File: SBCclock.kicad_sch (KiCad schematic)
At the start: 12 parts, among them J1 Conn_01x06_Male, J2 Conn_01x06_Male, U1 74HCT04, U2 74HC163, U3 74AHC1G02, Y1 25.175MHz

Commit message: chore: tweak values
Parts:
- C2: value 18pF -> 1uF
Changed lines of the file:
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@@
       (effects (font (size 1.27 1.27)))
     )
-    (property "Value" "18pF" (at 130.1496 98.0948 90)
+    (property "Value" "1uF" (at 130.1496 98.0948 90)
       (effects (font (size 1.27 1.27)))
     )

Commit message: chore: adjust routing
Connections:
- net ~{RESET}: now reaches J2.4 (Pin_4)
- no-connect marks 8 -> 7
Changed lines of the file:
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@@
   (no_connect (at 121.2596 118.6688))
   (no_connect (at 146.6596 123.7488))
-  (no_connect (at 253.0856 41.4528))
   (wire (pts (xy 86.3092 47.498) (xy 86.3092 60.7568))
     (stroke (width 0) (type default))
@@
       (effects (font (size 1.27 1.27)) (justify left) hide)
     )
+  )
+  (global_label "~{RESET}" (shape input) (at 253.0856 41.4528 0) (fields_autoplaced)
+    (effects (font (size 1.27 1.27)) (justify left))
+    (property "Intersheetrefs" "${INTERSHEET_REFS}" (at 261.7365 41.4528 0)
+      (effects (font (size 1.27 1.27)) (justify left) hide)
+    )

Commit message: revise E generation
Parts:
- added C3: 1uF, Capacitor_SMD:C_0805_2012Metric_Pad1.18x1.45mm_HandSolder, symbol Device:C
- added D1: LED, LED_SMD:LED_0805_2012Metric_Pad1.15x1.40mm_HandSolder, symbol Device:LED_Small_Filled
- added R5: 330R, Resistor_SMD:R_0805_2012Metric_Pad1.20x1.40mm_HandSolder, symbol Device:R_Small
- added U4: 74AHC1G08, Package_TO_SOT_SMD:SOT-353_SC-70-5_Handsoldering, symbol 74xGxx:74AHC1G08
- added U5: 74AHC1G32, Package_TO_SOT_SMD:SOT-353_SC-70-5_Handsoldering, symbol 74xGxx:74AHC1G32
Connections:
- net +5V: now also C3.1, R5.2, U4.5 (VCC), U5.5 (VCC)
- net Clock3: now also U4.1
- net Clock6: now also U4.2
- net E: now also U5.4; no longer U3.4
- net GND: now also C3.2, D1.1 (K), U4.3 (GND), U5.3 (GND)
- net at C1.2, R1.1, R2.1: now also U1.3; no longer U1.1
- net at R2.2, Y1.1: now also U1.4; no longer U1.2
- net at C1.1, R3.2, U1.5: now also U1.2; no longer U1.4
- net at R3.1, Y1.2: now also U1.1; no longer U1.3
- new net: D1.2 (A), R5.1
- new net: U3.4, U5.1
- new net: U4.4, U5.2
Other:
- moved on the sheet: U3

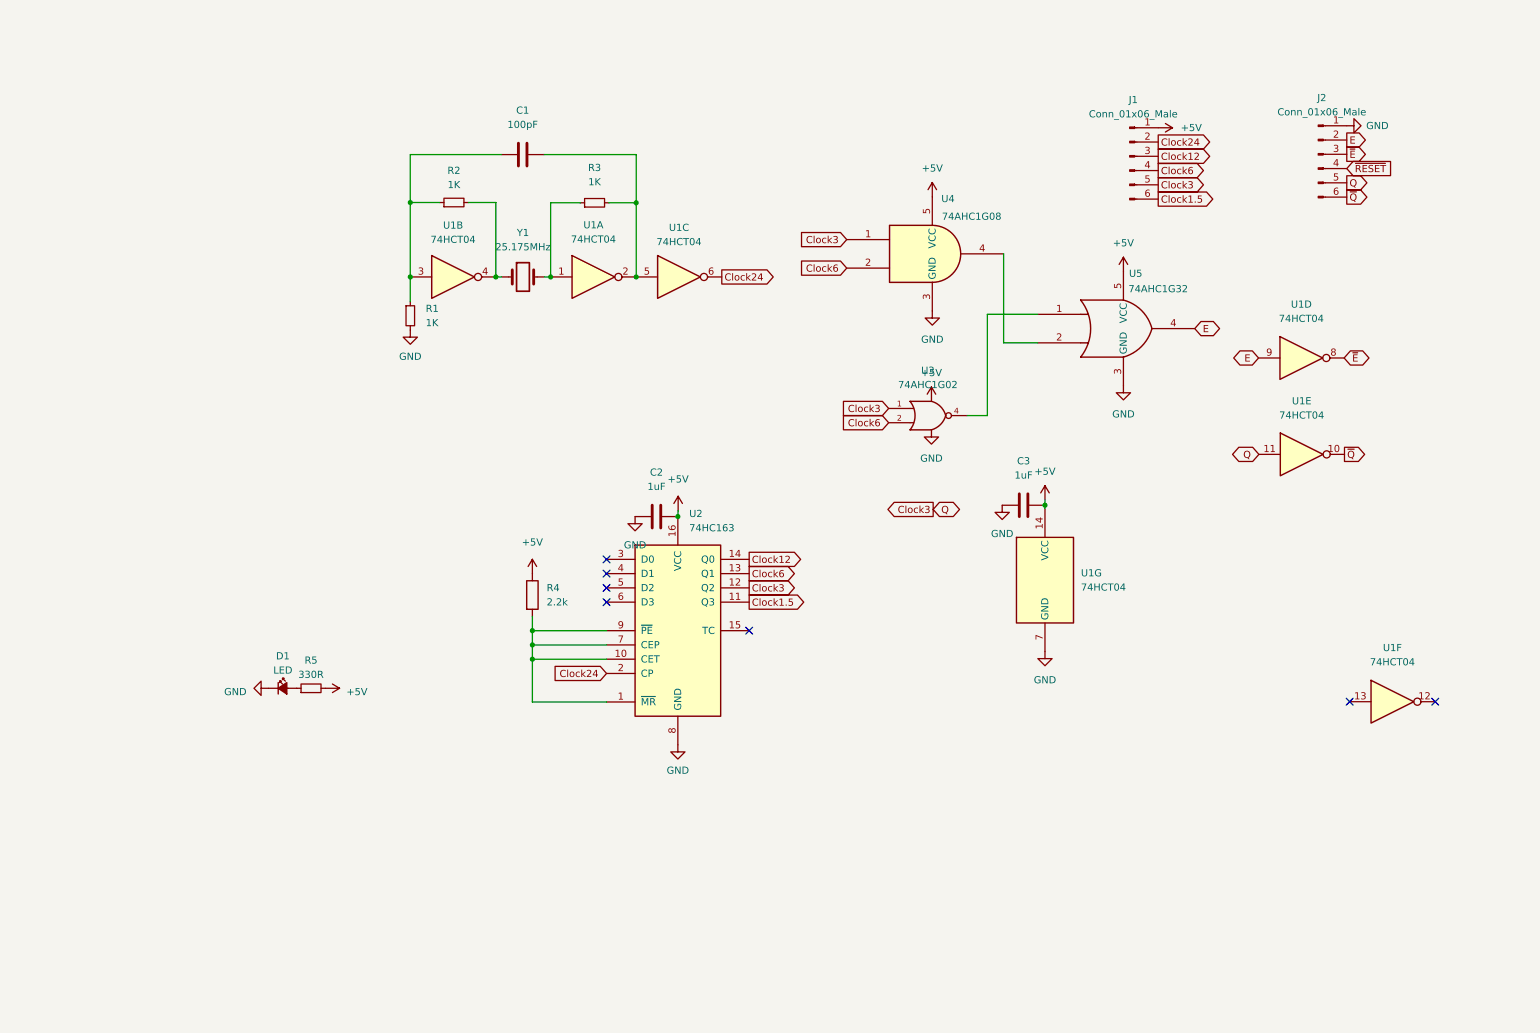
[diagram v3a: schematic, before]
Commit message: simplified board
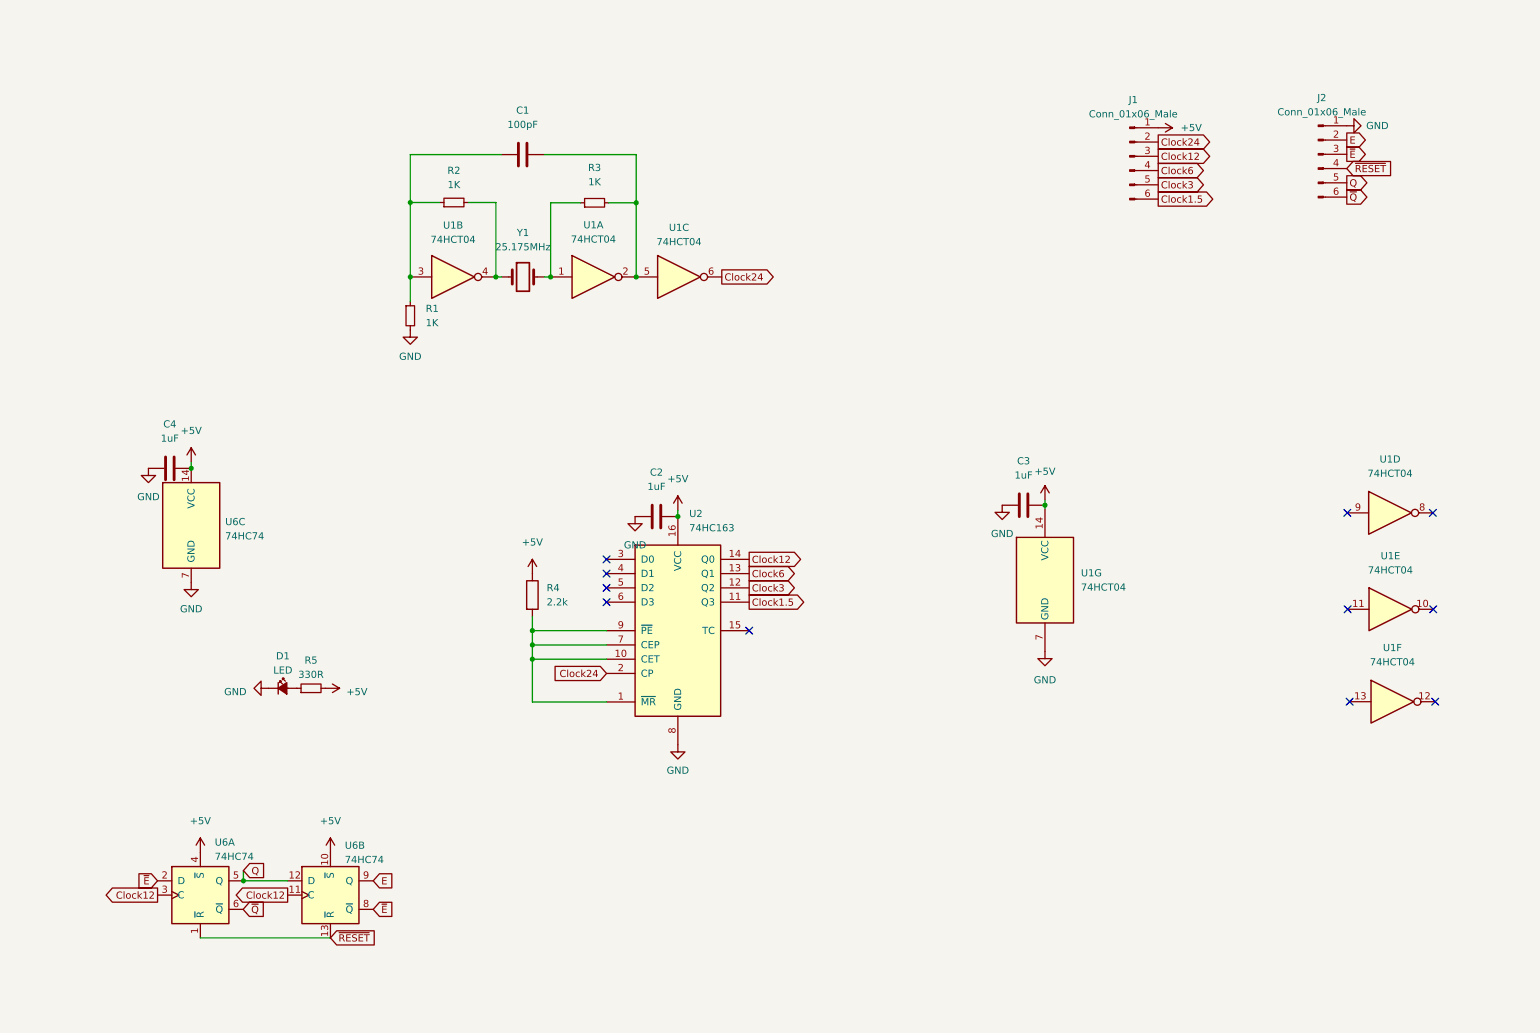
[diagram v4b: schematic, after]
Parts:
- removed U3: 74AHC1G02, Package_TO_SOT_SMD:SOT-353_SC-70-5_Handsoldering, symbol 74xGxx:74AHC1G02
- removed U4: 74AHC1G08, Package_TO_SOT_SMD:SOT-353_SC-70-5_Handsoldering, symbol 74xGxx:74AHC1G08
- removed U5: 74AHC1G32, Package_TO_SOT_SMD:SOT-353_SC-70-5_Handsoldering, symbol 74xGxx:74AHC1G32
- added C4: 1uF, Capacitor_SMD:C_0805_2012Metric_Pad1.18x1.45mm_HandSolder, symbol Device:C
- added U6: 74HC74, Package_SO:SOIC-14_3.9x8.7mm_P1.27mm, symbol 74xx:74HC74
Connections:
- net +5V: now also C4.1, U6.10 (~{S}), U6.14 (VCC), U6.4 (~{S})
- net Clock12: now also U6.11 (C), U6.3 (C)
- net Clock3: no longer J2.5 (Pin_5), U1.11
- net E: now also U6.9 (Q); no longer U1.9
- net GND: now also C4.2, U6.7 (GND)
- net ~{E}: now also U6.2 (D), U6.8 (~{Q}); no longer U1.8
- net ~{Q}: now also U6.6 (~{Q}); no longer U1.10
- net ~{RESET}: now also U6.1 (~{R}), U6.13 (~{R})
- new net Q: J2.5 (Pin_5), U6.12 (D), U6.5 (Q)
- no-connect marks 7 -> 11
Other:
- moved on the sheet: U1D, U1E

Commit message: revise clock signal
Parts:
- removed R3: 1K, Resistor_SMD:R_0805_2012Metric_Pad1.20x1.40mm_HandSolder, symbol Device:R_Small
- removed U1: 74HCT04, Package_SO:SOIC-14_3.9x8.7mm_P1.27mm, symbol 74xx:74HCT04
- added C2: 22pF, Capacitor_SMD:C_0805_2012Metric_Pad1.18x1.45mm_HandSolder, symbol Device:C
- added D2: LED, LED_SMD:LED_0805_2012Metric_Pad1.15x1.40mm_HandSolder, symbol Device:LED_Small_Filled
- added JP1: SolderJumper_3_Bridged12, Jumper:SolderJumper-3_P1.3mm_Bridged12_Pad1.0x1.5mm, symbol Jumper:SolderJumper_3_Bridged12
- added R5: 330R, Resistor_SMD:R_0805_2012Metric_Pad1.20x1.40mm_HandSolder, symbol Device:R_Small
- added U1: 74HC14, Package_SO:SOIC-14_3.9x8.7mm_P1.27mm, symbol 74xx:74HC14
- C1: value 100pF -> 22pF
- R2: value 1K -> 1M
- U2: value 74HC163 -> 74HCT163
- U3: renamed from U6; value 74HC74 -> 74HCT74
- renumbered C2 to C5, R4 to R3, R5 to R4
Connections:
- net +5V: now also U1.14 (VCC)
- net Clock12: now also JP1.1 (A); no longer U3.11 (C), U3.3 (C)
- net Clock24: now also U1.4
- net Clock6: now also JP1.3 (B)
- net GND: now also C1.1, C2.1, D2.1 (K), U1.7 (GND); no longer R1.2
- net ~{RESET}: now also U1.11; no longer U3.1 (~{R}), U3.13 (~{R})
- net at C1.2, R2.1: now also Y1.1, U1.1; no longer R1.1
- net at R2.2: now also R1.2, U1.2, U1.3; no longer Y1.1
- net at Y1.2: now also R1.1, C2.2
- new net: D2.2 (A), R5.1
- new net: U1.8, U3.1 (~{R}), U3.13 (~{R})
- new net QuadC: JP1.2 (C), U3.11 (C), U3.3 (C)
- new net RESET: R5.2, U1.10, U1.9
- no-connect marks 11 -> 9
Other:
- note added: "Clock Divider Output at /2 /4 /8 and /16"
- note added: "Power"
- note added: "Provides Clock signal for video Quadrature signal for CPU(s)"
- note added: "Quadrature signal generator Operates at input /4 Outputs Q-E for CPU1 ~{Q}-~{E} for CPU2"
- note added: "Raw clock signal at TTL level"
- note added: "Reset (high)"
- note added: "Reset suspends quadrature outputs but not clock divider"
- moved on the sheet: C3, C4, C5, D1, R1, R2, R3, R4, U2, U3A, U3B, U3C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

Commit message: v2 board
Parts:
- removed J1, J2: Conn_01x06_Male, Connector_PinHeader_2.54mm:PinHeader_1x06_P2.54mm_Vertical, symbol Connector:Conn_01x06_Male
- removed JP1: SolderJumper_3_Bridged12, Jumper:SolderJumper-3_P1.3mm_Bridged12_Pad1.0x1.5mm, symbol Jumper:SolderJumper_3_Bridged12
- removed U3: 74HCT74, Package_SO:SOIC-14_3.9x8.7mm_P1.27mm, symbol 74xx:74HC74
- added C6: 1uF, Capacitor_SMD:C_0805_2012Metric_Pad1.18x1.45mm_HandSolder, symbol Device:C
- added J1, J2: Conn_01x07, Connector_PinHeader_2.54mm:PinHeader_1x07_P2.54mm_Vertical, symbol Connector_Generic:Conn_01x07
- added U3: 74HCT112, Package_SO:SOIC-16_3.9x9.9mm_P1.27mm, symbol 74xx:74LS112
- added U5: 74HCT153, Package_SO:SOIC-16_3.9x9.9mm_P1.27mm, symbol 74xx:74LS153
- U1: value 74HC14 -> 74HCT14; DigiKey (none) -> 296-14864-1-ND
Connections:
- net +5V: now also C6.1, J2.7 (Pin_7), U3.10 (~{S}), U3.16 (VCC), U3.4 (~{S}), U5.15 (Eb), U5.16 (VCC)
- net Clock1.5: now also J1.7 (Pin_7), U5.3 (I3a)
- net Clock12: now also J1.4 (Pin_4), U5.6 (I0a)
- net Clock24: now also J1.3 (Pin_3)
- net Clock3: now also J1.6 (Pin_6), U5.4 (I2a)
- net Clock6: now also J1.5 (Pin_5), U5.5 (I1a)
- net E: now also U1.12, J2.2 (Pin_2)
- net GND: now also C6.2, J2.1 (Pin_1), U3.8 (GND), U5.1 (Ea), U5.8 (GND)
- net Q: now also U1.6, J2.5 (Pin_5)
- net QuadC: now also U3.1 (C), U3.13 (C), U5.7 (Za)
- net ~{E}: now also U1.13, J2.3 (Pin_3), U3.3 (J), U3.7 (~{Q})
- net ~{Q}: now also U1.5, J2.6 (Pin_6), U3.12 (K), U3.6 (~{Q})
- net ~{RESET}: now also J2.4 (Pin_4)
- net at U1.8: now also U3.14 (~{R}), U3.15 (~{R})
- new net: U3.2 (K), U3.9 (Q)
- new net: U3.11 (J), U3.5 (Q)
- new net SEL0: J1.1 (Pin_1), U5.14 (S0)
- new net SEL1: J1.2 (Pin_2), U5.2 (S1)
- no-connect marks 9 -> 10
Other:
- moved on the sheet: C1, C2, D1, D2, R1, R2, R4, R5, U1A, U1B, U1C, U1D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

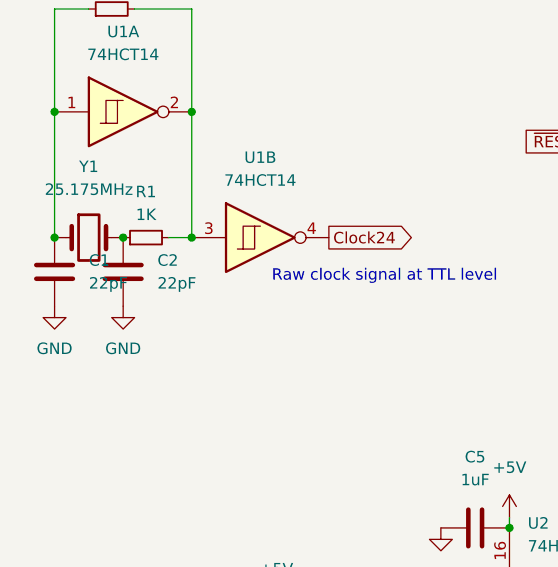
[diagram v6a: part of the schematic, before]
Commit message: revise load capacitors
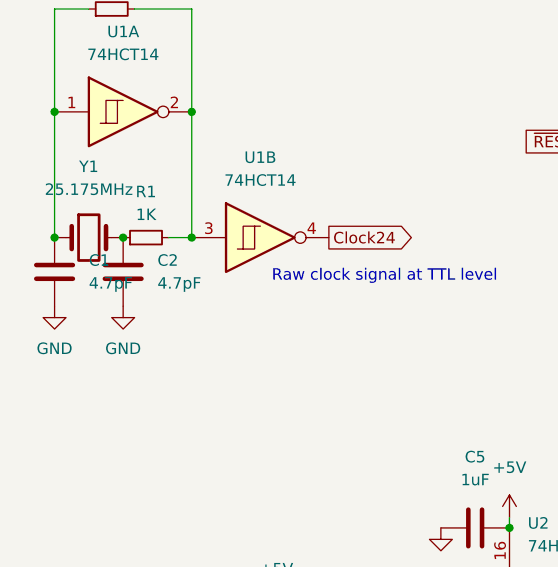
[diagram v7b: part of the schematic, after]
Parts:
- C1, C2: value 22pF -> 4.7pF
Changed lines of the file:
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@@
       (effects (font (size 1.27 1.27)) hide)
     )
+    (pin "1")
+    (pin "15")
+    (pin "2")
+    (pin "3")
+    (pin "4")
+    (pin "5")
+    (pin "6")
+    (pin "10")
+    (pin "11")
+    (pin "12")
+    (pin "13")
+    (pin "14")
+    (pin "7")
+    (pin "9")
+    (pin "16")
     (pin "8")
-    (pin "5")
-    (pin "1")
+    (instances
+      (project "SBCclock"
+        (path "/261b8f07-acf7-48ee-8a25-93f738c9b1c6"
+          (reference "U3") (unit 3)
+        )
+      )
+    )
+  )
+  (symbol (lib_id "power:GND") (at 208.2292 152.8572 0) (unit 1)
+    (in_bom yes) (on_board yes) (dnp no) (fields_autoplaced)
+    (property "Reference" "#PWR09" (at 208.2292 159.2072 0)
+      (effects (font (size 1.27 1.27)) hide)
+    )
+    (property "Value" "GND" (at 208.2292 157.9372 0)
+      (effects (font (size 1.27 1.27)))
+    )
+    (property "Footprint" "" (at 208.2292 152.8572 0)
+      (effects (font (size 1.27 1.27)) hide)
+    )
+    (property "Datasheet" "" (at 208.2292 152.8572 0)
+      (effects (font (size 1.27 1.27)) hide)
+    )
+    (pin "1")
+    (instances
+      (project "SBCclock"
+        (path "/261b8f07-acf7-48ee-8a25-93f738c9b1c6"
+          (reference "#PWR09") (unit 1)
+        )
+      )
+    )
+  )
+  (symbol (lib_id "74xx:74LS153") (at 160.274 118.872 0) (unit 1)
+    (in_bom yes) (on_board yes) (dnp no) (fields_autoplaced)
+    (property "Reference" "U5" (at 162.4681 93.218 0)
+      (effects (font (size 1.27 1.27)) (justify left))
+    )
+    (property "Value" "74HCT153" (at 162.4681 95.758 0)
+      (effects (font (size 1.27 1.27)) (justify left))
+    )
+    (property "Footprint" "Package_SO:SOIC-16_3.9x9.9mm_P1.27mm" (at 160.274 118.872 0)
+      (effects (font (size 1.27 1.27)) hide)
+    )
+    (property "Datasheet" "http://www.ti.com/lit/gpn/sn74LS153" (at 160.274 118.872 0)
+      (effects (font (size 1.27 1.27)) hide)
+    )
+    (property "DigiKey" "296-CD74HCT153M96CT-ND" (at 160.274 118.872 0)
+      (effects (font (size 1.27 1.27)) hide)
+    )
+    (pin "1")
+    (pin "10")
+    (pin "11")
+    (pin "12")
     (pin "13")
-    (pin "7")
-    (pin "12")
-    (pin "10")
-    (pin "9")
-    (pin "15")
-    (pin "6")
-    (pin "16")
-    (pin "2")
     (pin "14")
-    (pin "4")
-    (pin "3")
-    (pin "11")
-    (instances
-      (project "SBCclock"
-        (path "/261b8f07-acf7-48ee-8a25-93f738c9b1c6"
-          (reference "U3") (unit 3)
-        )
-      )
-    )
-  )
-  (symbol (lib_id "power:GND") (at 208.2292 152.8572 0) (unit 1)
-    (in_bom yes) (on_board yes) (dnp no) (fields_autoplaced)
-    (property "Reference" "#PWR09" (at 208.2292 159.2072 0)
-      (effects (font (size 1.27 1.27)) hide)
-    )
-    (property "Value" "GND" (at 208.2292 157.9372 0)
-      (effects (font (size 1.27 1.27)))
-    )
-    (property "Footprint" "" (at 208.2292 152.8572 0)
-      (effects (font (size 1.27 1.27)) hide)
-    )
-    (property "Datasheet" "" (at 208.2292 152.8572 0)
-      (effects (font (size 1.27 1.27)) hide)
-    )
-    (pin "1")
-    (instances
-      (project "SBCclock"
-        (path "/261b8f07-acf7-48ee-8a25-93f738c9b1c6"
-          (reference "#PWR09") (unit 1)
-        )
-      )
-    )
-  )
-  (symbol (lib_id "74xx:74LS153") (at 160.274 118.872 0) (unit 1)
-    (in_bom yes) (on_board yes) (dnp no) (fields_autoplaced)
-    (property "Reference" "U5" (at 162.4681 93.218 0)
-      (effects (font (size 1.27 1.27)) (justify left))
-    )
-    (property "Value" "74HCT153" (at 162.4681 95.758 0)
-      (effects (font (size 1.27 1.27)) (justify left))
-    )
-    (property "Footprint" "Package_SO:SOIC-16_3.9x9.9mm_P1.27mm" (at 160.274 118.872 0)
-      (effects (font (size 1.27 1.27)) hide)
-    )
-    (property "Datasheet" "http://www.ti.com/lit/gpn/sn74LS153" (at 160.274 118.872 0)
-      (effects (font (size 1.27 1.27)) hide)
-    )
-    (property "DigiKey" "296-CD74HCT153M96CT-ND" (at 160.274 118.872 0)
-      (effects (font (size 1.27 1.27)) hide)
-    )
     (pin "15")
     (pin "16")
-    (pin "10")
-    (pin "7")
+    (pin "2")
+    (pin "3")
+    (pin "4")
     (pin "5")
     (pin "6")
-    (pin "12")
+    (pin "7")
     (pin "8")
     (pin "9")
-    (pin "3")
-    (pin "13")
-    (pin "2")
-    (pin "11")
-    (pin "4")
-    (pin "1")
-    (pin "14")
     (instances
       (project "SBCclock"
@@
       (effects (font (size 1.27 1.27)) hide)
     )
+    (pin "1")
+    (pin "15")
+    (pin "2")
+    (pin "3")
+    (pin "4")
+    (pin "5")
+    (pin "6")
+    (pin "10")
+    (pin "11")
+    (pin "12")
+    (pin "13")
+    (pin "14")
+    (pin "7")
+    (pin "9")
+    (pin "16")
     (pin "8")
-    (pin "5")
-    (pin "1")
-    (pin "13")
-    (pin "7")
-    (pin "12")
-    (pin "10")
-    (pin "9")
-    (pin "15")
-    (pin "6")
-    (pin "16")
-    (pin "2")
-    (pin "14")
-    (pin "4")
-    (pin "3")
-    (pin "11")
     (instances
       (project "SBCclock"
@@
       (effects (font (size 1.27 1.27)) (justify right))
     )
-    (property "Value" "22pF" (at 23.114 62.992 0)
+    (property "Value" "4.7pF" (at 23.114 62.992 0)
       (effects (font (size 1.27 1.27)) (justify right))
     )
@@
       (effects (font (size 1.27 1.27)) hide)
     )
+    (pin "1")
+    (pin "2")
+    (pin "3")
     (pin "4")
+    (pin "5")
     (pin "6")
+    (pin "7")
+    (instances
+      (project "SBCclock"
+        (path "/261b8f07-acf7-48ee-8a25-93f738c9b1c6"
+          (reference "J1") (unit 1)
+        )
+      )
+    )
+  )
+  (symbol (lib_id "74xx:74LS112") (at 149.352 36.83 0) (unit 2)
+    (in_bom yes) (on_board yes) (dnp no) (fields_autoplaced)
+    (property "Reference" "U3" (at 151.5461 27.178 0)
+      (effects (font (size 1.27 1.27)) (justify left))
+    )
+    (property "Value" "74HCT112" (at 151.5461 29.718 0)
+      (effects (font (size 1.27 1.27)) (justify left))
+    )
+    (property "Footprint" "Package_SO:SOIC-16_3.9x9.9mm_P1.27mm" (at 149.352 36.83 0)
+      (effects (font (size 1.27 1.27)) hide)
+    )
+    (property "Datasheet" "http://www.ti.com/lit/gpn/sn74LS112" (at 149.352 36.83 0)
+      (effects (font (size 1.27 1.27)) hide)
+    )
+    (property "DigiKey" "1727-74HCT112D,653CT-ND" (at 149.352 36.83 0)
+      (effects (font (size 1.27 1.27)) hide)
+    )
+    (pin "1")
+    (pin "15")
+    (pin "2")
+    (pin "3")
+    (pin "4")
     (pin "5")
-    (pin "2")
-    (pin "3")
+    (pin "6")
+    (pin "10")
+    (pin "11")
+    (pin "12")
+    (pin "13")
+    (pin "14")
     (pin "7")
-    (pin "1")
-    (instances
-      (project "SBCclock"
-        (path "/261b8f07-acf7-48ee-8a25-93f738c9b1c6"
-          (reference "J1") (unit 1)
-        )
-      )
-    )
-  )
-  (symbol (lib_id "74xx:74LS112") (at 149.352 36.83 0) (unit 2)
-    (in_bom yes) (on_board yes) (dnp no) (fields_autoplaced)
-    (property "Reference" "U3" (at 151.5461 27.178 0)
-      (effects (font (size 1.27 1.27)) (justify left))
-    )
-    (property "Value" "74HCT112" (at 151.5461 29.718 0)
-      (effects (font (size 1.27 1.27)) (justify left))
-    )
-    (property "Footprint" "Package_SO:SOIC-16_3.9x9.9mm_P1.27mm" (at 149.352 36.83 0)
-      (effects (font (size 1.27 1.27)) hide)
-    )
-    (property "Datasheet" "http://www.ti.com/lit/gpn/sn74LS112" (at 149.352 36.83 0)
-      (effects (font (size 1.27 1.27)) hide)
-    )
-    (property "DigiKey" "1727-74HCT112D,653CT-ND" (at 149.352 36.83 0)
-      (effects (font (size 1.27 1.27)) hide)
-    )
+    (pin "9")
+    (pin "16")
     (pin "8")
-    (pin "5")
-    (pin "1")
-    (pin "13")
-    (pin "7")
-    (pin "12")
-    (pin "10")
-    (pin "9")
-    (pin "15")
-    (pin "6")
-    (pin "16")
-    (pin "2")
-    (pin "14")
-    (pin "4")
-    (pin "3")
-    (pin "11")
     (instances
       (project "SBCclock"
@@
     )
     (pin "1")
+    (pin "2")
     (pin "3")
-    (pin "6")
-    (pin "2")
-    (pin "7")
     (pin "4")
     (pin "5")
+    (pin "6")
+    (pin "7")
     (instances
       (project "SBCclock"
@@
       (effects (font (size 1.27 1.27)) (justify right))
     )
-    (property "Value" "22pF" (at 30.734 62.992 0)
+    (property "Value" "4.7pF" (at 30.734 62.992 0)
       (effects (font (size 1.27 1.27)) (justify right))
     )
